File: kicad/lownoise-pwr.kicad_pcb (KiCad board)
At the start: 2 copper layers, 78 x 36.9 mm, 27 parts, among them J1 Conn_01x02_Female, J2 Conn_01x02_Female, J3 Conn_01x02_Female, Q1 BD244C, U1 LM723_DIP14, U2 LM4040DBZ-4.1

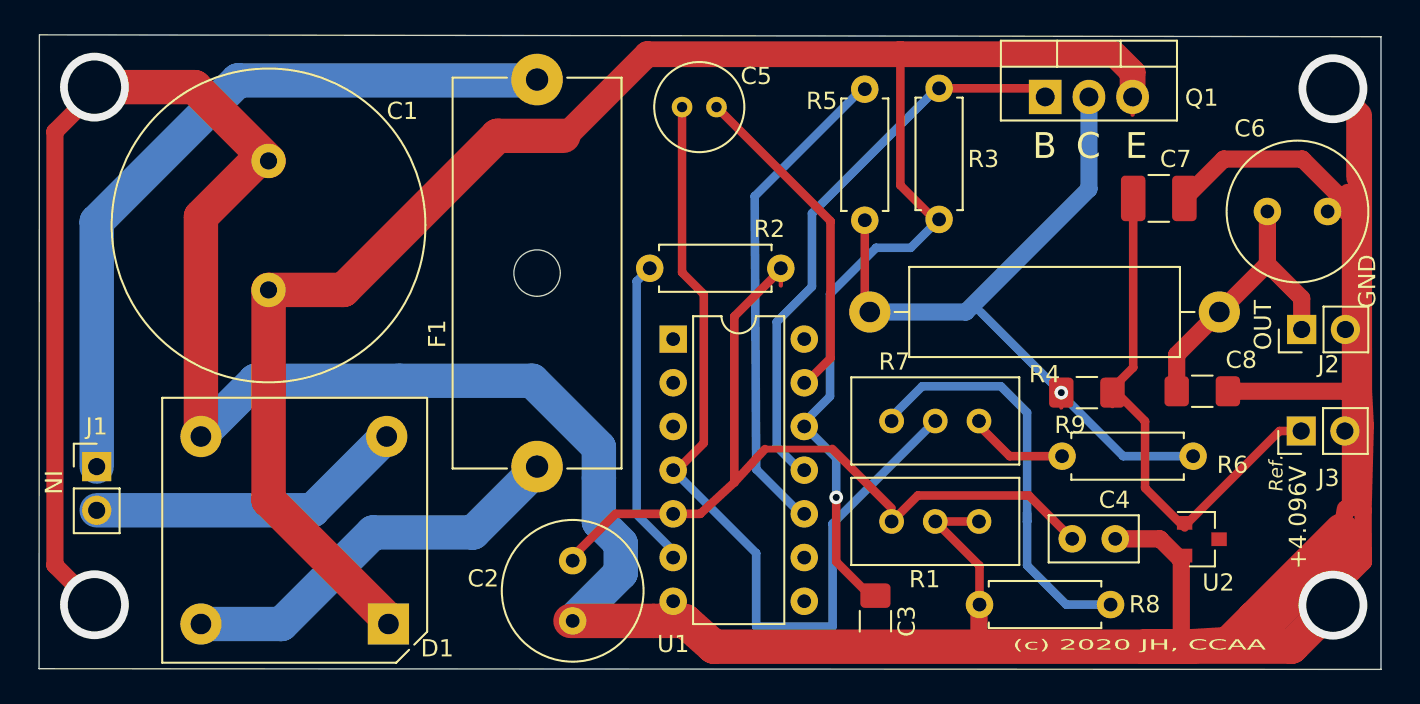
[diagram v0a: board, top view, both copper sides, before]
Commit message: Enlarge power pins in and out
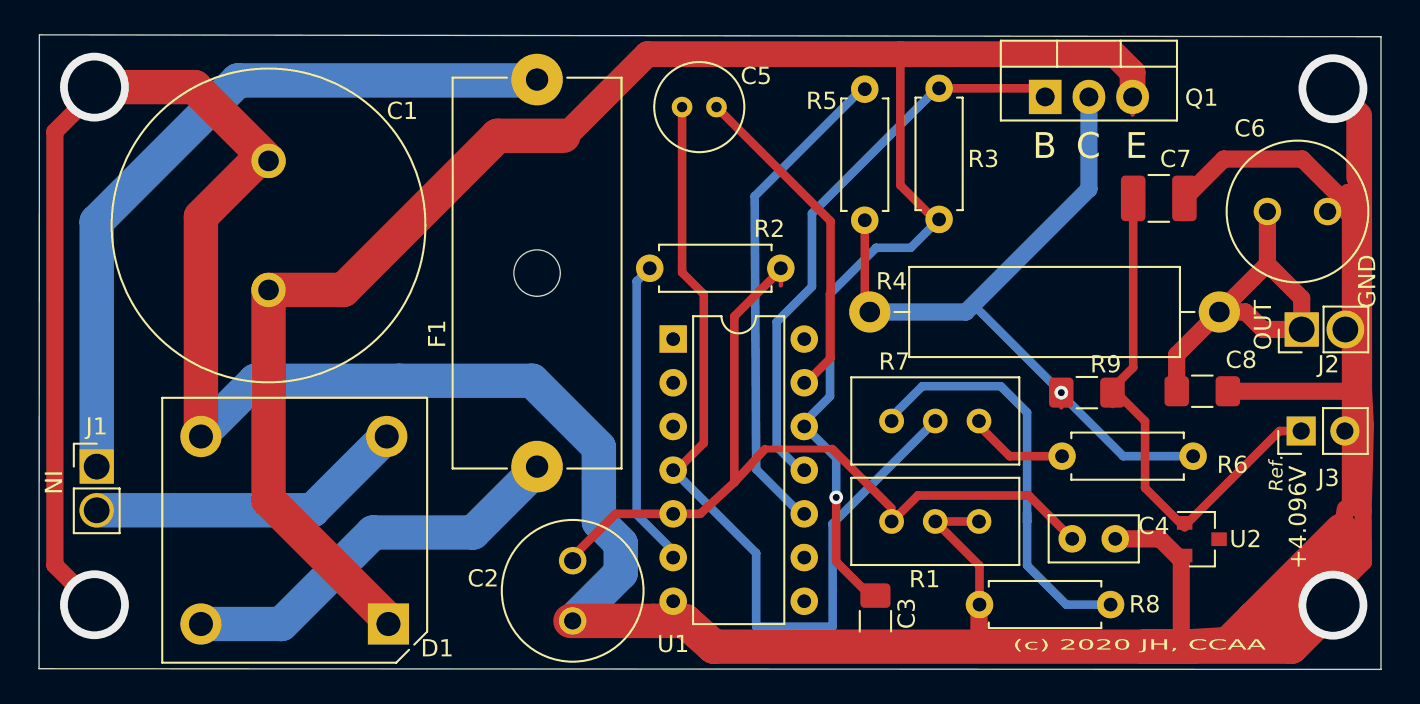
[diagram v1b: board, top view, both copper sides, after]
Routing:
- net Net-(C6-Pad1): track 17.9 -> 23.1 mm
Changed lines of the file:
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@@
     (thickness 1.6)
     (drawings 17)
-    (tracks 242)
+    (tracks 245)
     (zones 0)
     (modules 27)
@@
     (mod_text_size 1 1)
     (mod_text_width 0.15)
-    (pad_size 1.524 1.524)
-    (pad_drill 0.762)
+    (pad_size 2 2)
+    (pad_drill 1.5)
     (pad_to_mask_clearance 0.051)
     (solder_mask_min_width 0.25)
@@
     (descr "Resistor, Axial_DIN0516 series, Axial, Horizontal, pin pitch=20.32mm, 2W, length*diameter=15.5*5mm^2, http://cdn-reichelt.de/documents/datenblatt/B400/1_4W%23YAG.pdf")
     (tags "Resistor Axial_DIN0516 series Axial Horizontal pin pitch 20.32mm 2W length 15.5mm diameter 5mm")
-    (fp_text reference R4 (at 10.16 -3.62) (layer F.SilkS)
+    (fp_text reference R4 (at 19.05 1.778) (layer F.SilkS)
       (effects (font (size 1 1) (thickness 0.15)))
     )
@@
     (tags "resistor handsolder")
     (attr smd)
-    (fp_text reference R9 (at -0.9775 1.88) (layer F.SilkS)
+    (fp_text reference R9 (at 1.0955 -1.64) (layer F.SilkS)
       (effects (font (size 1 1) (thickness 0.15)))
     )
@@
     (fp_line (start 13.15 13.15) (end -2.25 13.15) (layer F.SilkS) (width 0.12))
     (fp_line (start -2.25 13.15) (end -2.25 -0.45) (layer F.SilkS) (width 0.12))
-    (pad 2 thru_hole circle (at 0.1 10.9) (size 2.4 2.4) (drill 1.2) (layers *.Cu *.Mask)
+    (pad 2 thru_hole circle (at 0.1 10.9) (size 2.4 2.4) (drill 1.4) (layers *.Cu *.Mask)
       (net 11 "Net-(D1-Pad2)"))
-    (pad 1 thru_hole rect (at 0 0) (size 2.4 2.4) (drill 1.2) (layers *.Cu *.Mask)
+    (pad 1 thru_hole rect (at 0 0) (size 2.4 2.4) (drill 1.4) (layers *.Cu *.Mask)
       (net 3 "Net-(C1-Pad1)"))
-    (pad 4 thru_hole circle (at 10.9 0) (size 2.4 2.4) (drill 1.2) (layers *.Cu *.Mask)
+    (pad 4 thru_hole circle (at 10.9 0) (size 2.4 2.4) (drill 1.4) (layers *.Cu *.Mask)
       (net 12 "Net-(D1-Pad4)"))
-    (pad 3 thru_hole circle (at 10.9 10.9) (size 2.4 2.4) (drill 1.2) (layers *.Cu *.Mask)
+    (pad 3 thru_hole circle (at 10.9 10.9) (size 2.4 2.4) (drill 1.4) (layers *.Cu *.Mask)
       (net 1 GND))
     (model ${KISYS3DMOD}/Diode_THT.3dshapes/Diode_Bridge_15.2x15.2x6.3mm_P10.9mm.wrl
@@
     (fp_circle (center 1.75 0) (end 5.87 0) (layer F.SilkS) (width 0.12))
     (fp_circle (center 1.75 0) (end 5.75 0) (layer F.Fab) (width 0.1))
-    (pad 2 thru_hole circle (at 3.5 0) (size 1.6 1.6) (drill 0.8) (layers *.Cu *.Mask)
+    (pad 2 thru_hole circle (at 3.5 0) (size 1.6 1.6) (drill 1) (layers *.Cu *.Mask)
       (net 1 GND))
-    (pad 1 thru_hole circle (at 0 0) (size 1.6 1.6) (drill 0.8) (layers *.Cu *.Mask)
+    (pad 1 thru_hole circle (at 0 0) (size 1.6 1.6) (drill 1) (layers *.Cu *.Mask)
       (net 9 "Net-(C6-Pad1)"))
     (model ${KISYS3DMOD}/Capacitor_THT.3dshapes/C_Radial_D8.0mm_H11.5mm_P3.50mm.wrl
@@
     (descr "C, Disc series, Radial, pin pitch=2.50mm, , diameter*width=5*2.5mm^2, Capacitor, http://cdn-reichelt.de/documents/datenblatt/B300/DS_KERKO_TC.pdf")
     (tags "C Disc series Radial pin pitch 2.50mm  diameter 5mm width 2.5mm Capacitor")
-    (fp_text reference C4 (at 2.456 -2.266) (layer F.SilkS)
+    (fp_text reference C4 (at 4.742 -0.742) (layer F.SilkS)
       (effects (font (size 1 1) (thickness 0.15)))
     )
@@
     (tags "capacitor handsolder")
     (attr smd)
-    (fp_text reference C3 (at 0 -1.82 90) (layer F.SilkS)
+    (fp_text reference C3 (at -0.4495 -1.82 90) (layer F.SilkS)
       (effects (font (size 1 1) (thickness 0.15)))
     )
@@
     (tags SOT-23)
     (attr smd)
-    (fp_text reference U2 (at 0.958 2.524) (layer F.SilkS)
+    (fp_text reference U2 (at 2.54 0) (layer F.SilkS)
       (effects (font (size 1 1) (thickness 0.15)))
     )
@@
     (fp_circle (center 1.75 0) (end 5.87 0) (layer F.SilkS) (width 0.12))
     (fp_circle (center 1.75 0) (end 5.75 0) (layer F.Fab) (width 0.1))
-    (pad 2 thru_hole circle (at 3.5 0 270) (size 1.6 1.6) (drill 0.8) (layers *.Cu *.Mask)
+    (pad 2 thru_hole circle (at 3.5 0 270) (size 1.6 1.6) (drill 1) (layers *.Cu *.Mask)
       (net 1 GND))
-    (pad 1 thru_hole circle (at 0 0 270) (size 1.6 1.6) (drill 0.8) (layers *.Cu *.Mask)
+    (pad 1 thru_hole circle (at 0 0 270) (size 1.6 1.6) (drill 1) (layers *.Cu *.Mask)
       (net 5 "Net-(C2-Pad1)"))
     (model ${KISYS3DMOD}/Capacitor_THT.3dshapes/C_Radial_D8.0mm_H7.0mm_P3.50mm.wrl
@@
     (fp_line (start 1.27 -1.27) (end 1.27 3.81) (layer F.Fab) (width 0.1))
     (fp_line (start -0.635 -1.27) (end 1.27 -1.27) (layer F.Fab) (width 0.1))
-    (pad 2 thru_hole oval (at 0 2.54 90) (size 1.7 1.7) (drill 1) (layers *.Cu *.Mask)
+    (pad 2 thru_hole oval (at 0 2.54 90) (size 2.2 2.2) (drill 1.5) (layers *.Cu *.Mask)
       (net 1 GND))
-    (pad 1 thru_hole rect (at 0 0 90) (size 1.7 1.7) (drill 1) (layers *.Cu *.Mask)
+    (pad 1 thru_hole rect (at 0 0 90) (size 2 2) (drill 1.5) (layers *.Cu *.Mask)
       (net 9 "Net-(C6-Pad1)"))
     (model ${KISYS3DMOD}/Connector_PinHeader_2.54mm.3dshapes/PinHeader_1x02_P2.54mm_Vertical.wrl
@@
     (fp_line (start 1.27 -1.27) (end 1.27 3.81) (layer F.Fab) (width 0.1))
     (fp_line (start -0.635 -1.27) (end 1.27 -1.27) (layer F.Fab) (width 0.1))
-    (pad 2 thru_hole oval (at 0 2.54) (size 1.7 1.7) (drill 1) (layers *.Cu *.Mask)
+    (pad 2 thru_hole oval (at 0 2.54) (size 2 2) (drill 1.5) (layers *.Cu *.Mask)
       (net 11 "Net-(D1-Pad2)"))
-    (pad 1 thru_hole rect (at 0 0) (size 1.7 1.7) (drill 1) (layers *.Cu *.Mask)
+    (pad 1 thru_hole rect (at 0 0) (size 2 2) (drill 1.5) (layers *.Cu *.Mask)
       (net 13 "Net-(F1-Pad1)"))
     (model ${KISYS3DMOD}/Connector_PinHeader_2.54mm.3dshapes/PinHeader_1x02_P2.54mm_Vertical.wrl
@@
     (fp_circle (center 3.75 0) (end 12.87 0) (layer F.SilkS) (width 0.12))
     (fp_circle (center 3.75 0) (end 12.75 0) (layer F.Fab) (width 0.1))
-    (pad 2 thru_hole circle (at 7.5 0 90) (size 2 2) (drill 1) (layers *.Cu *.Mask)
+    (pad 2 thru_hole circle (at 7.5 0 90) (size 2 2) (drill 1.2) (layers *.Cu *.Mask)
       (net 1 GND))
-    (pad 1 thru_hole circle (at 0 0 90) (size 2 2) (drill 1) (layers *.Cu *.Mask)
+    (pad 1 thru_hole circle (at 0 0 90) (size 2 2) (drill 1.2) (layers *.Cu *.Mask)
       (net 3 "Net-(C1-Pad1)"))
     (model ${KISYS3DMOD}/Capacitor_THT.3dshapes/C_Radial_D18.0mm_H35.5mm_P7.50mm.wrl
@@
   (segment (start 119.0372 75.146) (end 119.0372 76.962) (width 1) (layer F.Cu) (net 9))
   (segment (start 117.0492 73.158) (end 119.0372 75.146) (width 1) (layer F.Cu) (net 9))
+  (segment (start 114.2492 75.946) (end 115.7732 75.946) (width 1) (layer F.Cu) (net 9))
+  (segment (start 116.7892 76.962) (end 119.0372 76.962) (width 1) (layer F.Cu) (net 9))
+  (segment (start 115.7732 75.946) (end 116.7892 76.962) (width 1) (layer F.Cu) (net 9))
   (segment (start 108.0372 80.634) (end 108.0372 81.418) (width 0.25) (layer F.Cu) (net 10))
   (segment (start 112.0372 88.474) (end 112.0872 88.474) (width 0.25) (layer F.Cu) (net 10))
